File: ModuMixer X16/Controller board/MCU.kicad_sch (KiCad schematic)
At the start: 33 parts, among them U1 STM32U5F9NJHxQ

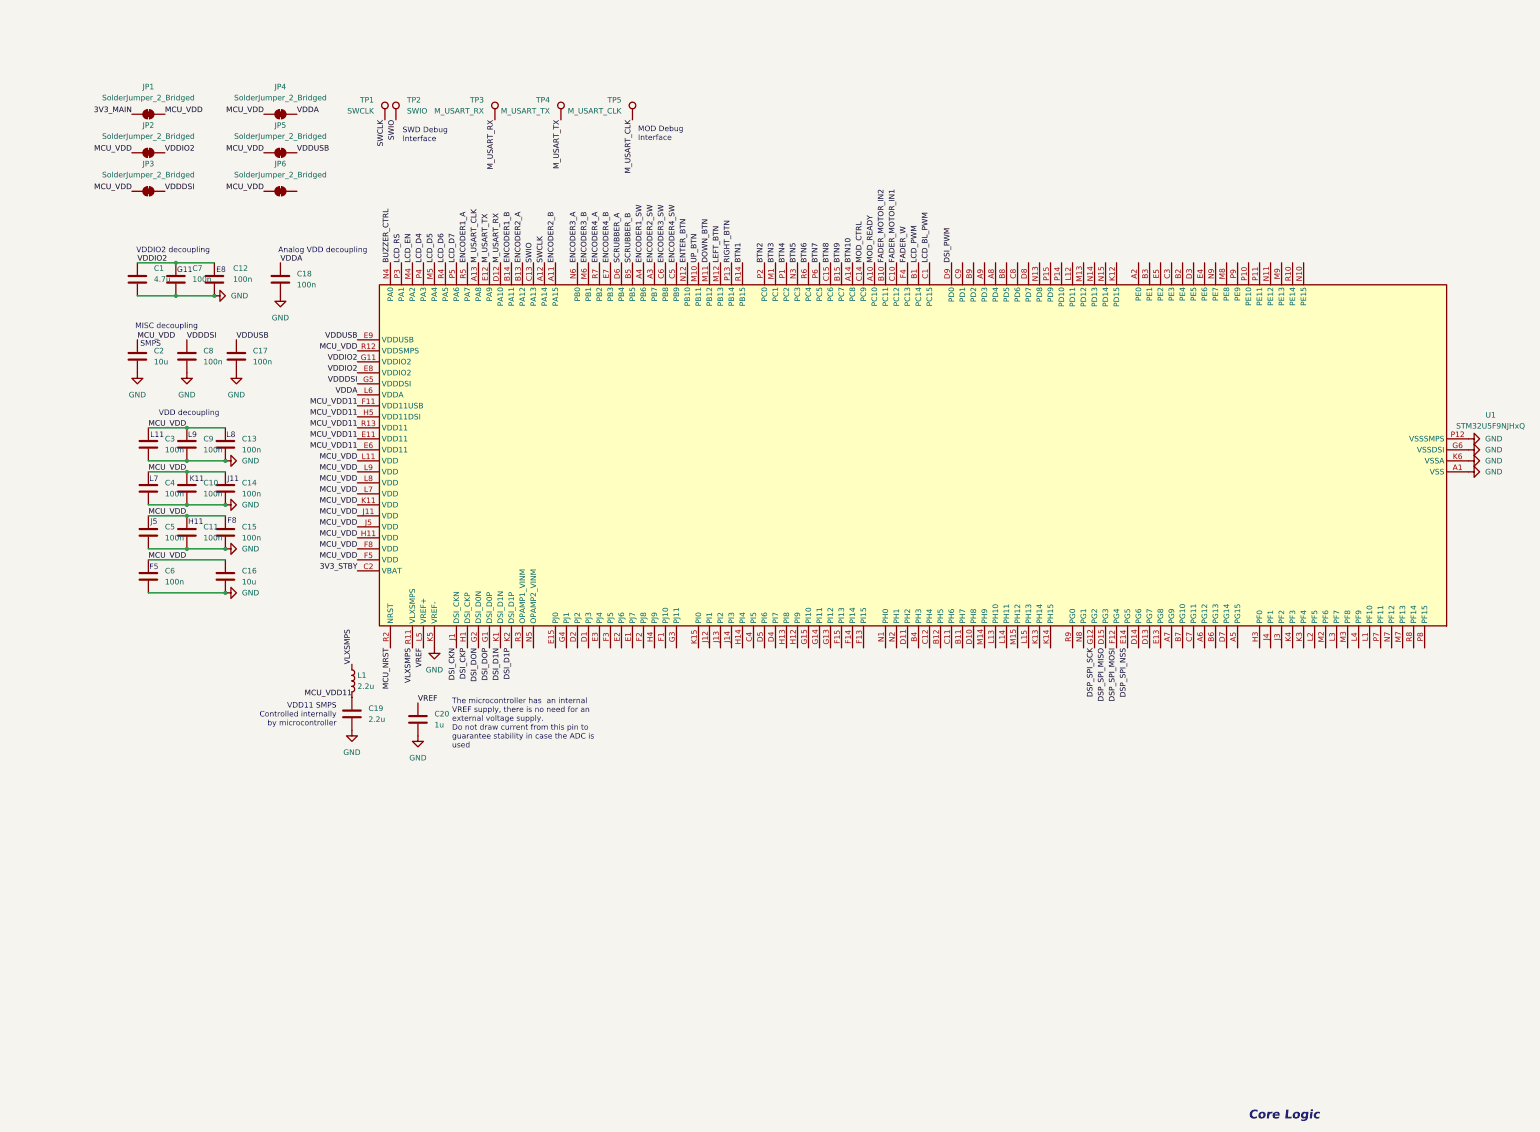
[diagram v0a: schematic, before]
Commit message: Switching microcontrollers
Midway through switching all microcontrollers in the project to STM32F103RC due to price constraints
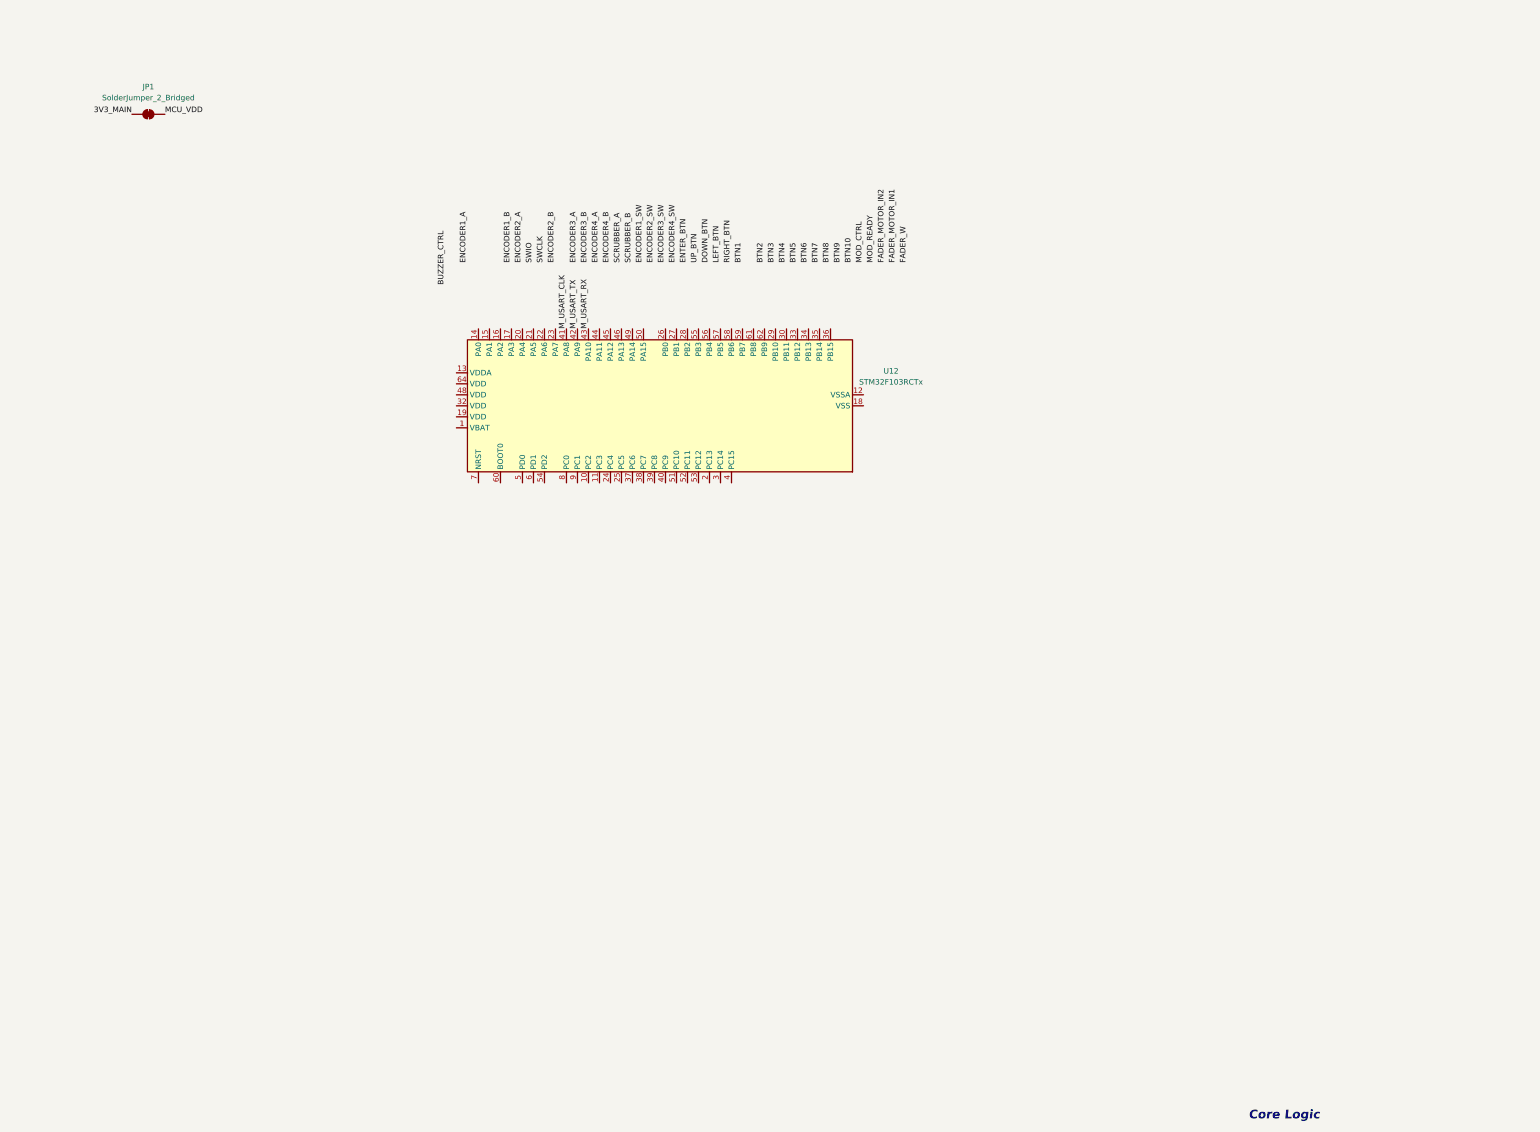
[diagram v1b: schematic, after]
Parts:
- removed C1: 4.7u, Capacitor_SMD:C_0603_1608Metric, symbol Device:C
- removed C10, C11, C12, C13, C14, C15, C17, C18, C3, C4, C5, C6, C7, C8, C9: 100n, Capacitor_SMD:C_0603_1608Metric, symbol Device:C
- removed C16, C2: 10u, Capacitor_SMD:C_0603_1608Metric, symbol Device:C
- removed C19: 2.2u, Capacitor_SMD:C_0603_1608Metric, symbol Device:C
- removed C20: 1u, Capacitor_SMD:C_0603_1608Metric, symbol Device:C
- removed JP2, JP3, JP4, JP5, JP6: SolderJumper_2_Bridged, Jumper:SolderJumper-2_P1.3mm_Bridged2Bar_Pad1.0x1.5mm, symbol Jumper:SolderJumper_2_Bridged
- removed L1: 2.2u, Capacitor_SMD:C_0603_1608Metric, symbol Device:L
- removed TP1: SWCLK, TestPoint:TestPoint_Pad_D3.0mm, symbol Connector:TestPoint
- removed TP2: SWIO, TestPoint:TestPoint_Pad_D3.0mm, symbol Connector:TestPoint
- removed TP3: M_USART_RX, TestPoint:TestPoint_Pad_D3.0mm, symbol Connector:TestPoint
- removed TP4: M_USART_TX, TestPoint:TestPoint_Pad_D3.0mm, symbol Connector:TestPoint
- removed TP5: M_USART_CLK, TestPoint:TestPoint_Pad_D3.0mm, symbol Connector:TestPoint
- removed U1: STM32U5F9NJHxQ, Package_BGA:TFBGA-216_13x13mm_Layout15x15_P0.8mm, symbol MCU_ST_STM32U5:STM32U5F9NJHxQ
- added U12: STM32F103RCTx, Package_QFP:LQFP-64_10x10mm_P0.5mm, symbol MCU_ST_STM32F1:STM32F103RCTx
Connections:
- net M_USART_CLK: now also U12.41 (PA8)
- net M_USART_RX: now also U12.43 (PA10)
- net M_USART_TX: now also U12.42 (PA9)
- new net: U12.18 (VSS), U12.31 (VSS), U12.47 (VSS), U12.63 (VSS)
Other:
- note removed: "Analog VDD decoupling"
- note removed: "E8"
- note removed: "F5"
- note removed: "F8"
- note removed: "G11"
- note removed: "H11"
- note removed: "J11"
- note removed: "J5"
- note removed: "K11"
- note removed: "L11"
- note removed: "L7"
- note removed: "L8"
- note removed: "L9"
- note removed: "MISC decoupling"
- note removed: "MOD Debug Interface"
- note removed: "SMPS"
- note removed: "SWD Debug Interface"
- note removed: "The microcontroller has an internal VREF supply, there is no need for an external voltage supply. Do not draw current from this pin to guarantee stability in case the ADC is used"
- note removed: "VDD decoupling"
- note removed: "VDD11 SMPS Controlled internally by microcontroller"
- note removed: "VDDIO2 decoupling"

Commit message: Midway through MCU change
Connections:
- net ENCODER1_A: now also U12.10 (PC2)
- net ENCODER1_B: now also U12.11 (PC3)
- net ENCODER1_SW: now also U12.61 (PB8)
- net ENCODER2_A: now also U12.24 (PC4)
- net ENCODER2_B: now also U12.25 (PC5)
- net ENCODER2_SW: now also U12.62 (PB9)
- net ENCODER3_A: now also U12.37 (PC6)
- net ENCODER3_B: now also U12.38 (PC7)
- net ENCODER3_SW: now also U12.29 (PB10)
- net ENCODER4_A: now also U12.39 (PC8)
- net ENCODER4_B: now also U12.40 (PC9)
- net ENCODER4_SW: now also U12.30 (PB11)
- net SCRUBBER_A: now also U12.8 (PC0)
- net SCRUBBER_B: now also U12.9 (PC1)
- net ENCODER6_B: now reaches U12.2 (PC13)
- net ENCODER7_A: now reaches U12.3 (PC14)
- net ENCODER5_SW: now reaches U12.33 (PB12)
- net ENCODER6_SW: now reaches U12.34 (PB13)
- net ENCODER7_SW: now reaches U12.35 (PB14)
- net ENCODER8_SW: now reaches U12.36 (PB15)
- net ENCODER7_B: now reaches U12.4 (PC15)
- net ENCODER5_A: now reaches U12.51 (PC10)
- net ENCODER5_B: now reaches U12.52 (PC11)
- net ENCODER6_A: now reaches U12.53 (PC12)
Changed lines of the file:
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@@
 	)
 	(label "ENCODER4_B"
-		(at 161.29 80.01 90)
-		(fields_autoplaced yes)
-		(effects
-			(font
-				(size 1.27 1.27)
-			)
-			(justify left bottom)
+		(at 173.99 130.81 270)
+		(fields_autoplaced yes)
+		(effects
+			(font
+				(size 1.27 1.27)
+			)
+			(justify right bottom)
 		)
 	)
 	(label "ENCODER2_A"
-		(at 140.97 80.01 90)
-		(fields_autoplaced yes)
-		(effects
-			(font
-				(size 1.27 1.27)
-			)
-			(justify left bottom)
+		(at 161.29 130.81 270)
+		(fields_autoplaced yes)
+		(effects
+			(font
+				(size 1.27 1.27)
+			)
+			(justify right bottom)
 		)
 	)
@@
 	)
 	(label "ENCODER1_B"
-		(at 138.43 80.01 90)
-		(fields_autoplaced yes)
-		(effects
-			(font
-				(size 1.27 1.27)
-			)
-			(justify left bottom)
+		(at 158.75 130.81 270)
+		(fields_autoplaced yes)
+		(effects
+			(font
+				(size 1.27 1.27)
+			)
+			(justify right bottom)
 		)
 	)
@@
 		)
 	)
+	(label "ENCODER5_B"
+		(at 179.07 130.81 270)
+		(fields_autoplaced yes)
+		(effects
+			(font
+				(size 1.27 1.27)
+			)
+			(justify right bottom)
+		)
+	)
 	(label "ENTER_BTN"
 		(at 179.07 80.01 90)
@@
 	)
 	(label "ENCODER3_A"
-		(at 153.67 80.01 90)
-		(fields_autoplaced yes)
-		(effects
-			(font
-				(size 1.27 1.27)
-			)
-			(justify left bottom)
+		(at 166.37 130.81 270)
+		(fields_autoplaced yes)
+		(effects
+			(font
+				(size 1.27 1.27)
+			)
+			(justify right bottom)
 		)
 	)
 	(label "ENCODER4_SW"
-		(at 176.53 80.01 90)
+		(at 201.93 95.25 90)
 		(fields_autoplaced yes)
 		(effects
@@
 	)
 	(label "ENCODER2_B"
-		(at 148.59 80.01 90)
-		(fields_autoplaced yes)
-		(effects
-			(font
-				(size 1.27 1.27)
-			)
-			(justify left bottom)
+		(at 163.83 130.81 270)
+		(fields_autoplaced yes)
+		(effects
+			(font
+				(size 1.27 1.27)
+			)
+			(justify right bottom)
 		)
 	)
 	(label "ENCODER2_SW"
-		(at 171.45 80.01 90)
+		(at 196.85 95.25 90)
 		(fields_autoplaced yes)
 		(effects
@@
 	)
 	(label "SCRUBBER_A"
-		(at 163.83 80.01 90)
-		(fields_autoplaced yes)
-		(effects
-			(font
-				(size 1.27 1.27)
-			)
-			(justify left bottom)
+		(at 151.13 130.81 270)
+		(fields_autoplaced yes)
+		(effects
+			(font
+				(size 1.27 1.27)
+			)
+			(justify right bottom)
 		)
 	)
@@
 		)
 	)
+	(label "ENCODER6_A"
+		(at 181.61 130.81 270)
+		(fields_autoplaced yes)
+		(effects
+			(font
+				(size 1.27 1.27)
+			)
+			(justify right bottom)
+		)
+	)
 	(label "BTN8"
 		(at 212.09 80.01 90)
@@
 	)
 	(label "ENCODER1_A"
-		(at 128.27 80.01 90)
-		(fields_autoplaced yes)
-		(effects
-			(font
-				(size 1.27 1.27)
-			)
-			(justify left bottom)
+		(at 156.21 130.81 270)
+		(fields_autoplaced yes)
+		(effects
+			(font
+				(size 1.27 1.27)
+			)
+			(justify right bottom)
 		)
 	)
@@
 		)
 	)
+	(label "ENCODER7_B"
+		(at 189.23 130.81 270)
+		(fields_autoplaced yes)
+		(effects
+			(font
+				(size 1.27 1.27)
+			)
+			(justify right bottom)
+		)
+	)
+	(label "ENCODER7_SW"
+		(at 209.55 95.25 90)
+		(fields_autoplaced yes)
+		(effects
+			(font
+				(size 1.27 1.27)
+			)
+			(justify left bottom)
+		)
+	)
 	(label "BTN2"
 		(at 196.85 80.01 90)
@@
 		)
 	)
+	(label "ENCODER6_SW"
+		(at 207.01 95.25 90)
+		(fields_autoplaced yes)
+		(effects
+			(font
+				(size 1.27 1.27)
+			)
+			(justify left bottom)
+		)
+	)
 	(label "BTN7"
 		(at 209.55 80.01 90)
@@
 	)
 	(label "ENCODER3_B"
-		(at 156.21 80.01 90)
-		(fields_autoplaced yes)
-		(effects
-			(font
-				(size 1.27 1.27)
-			)
-			(justify left bottom)
+		(at 168.91 130.81 270)
+		(fields_autoplaced yes)
+		(effects
+			(font
+				(size 1.27 1.27)
+			)
+			(justify right bottom)
 		)
 	)
@@
 		)
 	)
+	(label "ENCODER8_SW"
+		(at 212.09 95.25 90)
+		(fields_autoplaced yes)
+		(effects
+			(font
+				(size 1.27 1.27)
+			)
+			(justify left bottom)
+		)
+	)
+	(label "ENCODER5_A"
+		(at 176.53 130.81 270)
+		(fields_autoplaced yes)
+		(effects
+			(font
+				(size 1.27 1.27)
+			)
+			(justify right bottom)
+		)
+	)
 	(label "MCU_VDD"
 		(at 58.42 45.72 0)
@@
 		)
 	)
+	(label "ENCODER6_B"
+		(at 184.15 130.81 270)
+		(fields_autoplaced yes)
+		(effects
+			(font
+				(size 1.27 1.27)
+			)
+			(justify right bottom)
+		)
+	)
 	(label "SCRUBBER_B"
-		(at 166.37 80.01 90)
-		(fields_autoplaced yes)
-		(effects
-			(font
-				(size 1.27 1.27)
-			)
-			(justify left bottom)
+		(at 153.67 130.81 270)
+		(fields_autoplaced yes)
+		(effects
+			(font
+				(size 1.27 1.27)
+			)
+			(justify right bottom)
 		)
 	)
@@
 	)
 	(label "ENCODER1_SW"
-		(at 168.91 80.01 90)
+		(at 194.31 95.25 90)
 		(fields_autoplaced yes)
 		(effects
@@
 	)
 	(label "ENCODER4_A"
-		(at 158.75 80.01 90)
-		(fields_autoplaced yes)
-		(effects
-			(font
-				(size 1.27 1.27)
-			)
-			(justify left bottom)
+		(at 171.45 130.81 270)
+		(fields_autoplaced yes)
+		(effects
+			(font
+				(size 1.27 1.27)
+			)
+			(justify right bottom)
+		)
+	)
+	(label "ENCODER5_SW"
+		(at 204.47 95.25 90)
+		(fields_autoplaced yes)
+		(effects
+			(font
+				(size 1.27 1.27)
+			)
+			(justify left bottom)
+		)
+	)
+	(label "ENCODER7_A"
+		(at 186.69 130.81 270)
+		(fields_autoplaced yes)
+		(effects
+			(font
+				(size 1.27 1.27)
+			)
+			(justify right bottom)
 		)
 	)
@@
 	)
 	(label "ENCODER3_SW"
-		(at 173.99 80.01 90)
-		(fields_autoplaced yes)
-		(effects
+		(at 199.39 95.25 90)
+		(fields_autoplaced yes)
+		(effects
